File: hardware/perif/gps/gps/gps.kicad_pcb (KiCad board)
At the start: 2 copper layers, 37 x 53 mm, 5 parts, among them J1 Conn_01x20_Male, U1 M10578-A2

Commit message: started GPS board skeleton
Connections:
- U1 pad 10: Net-(J1-Pad16) -> Net-(J1-Pad17)
- U1 pad 9: Net-(J1-Pad17) -> Net-(J1-Pad16)
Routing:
- net Net-(J1-Pad17): track 4.81 -> 8.73 mm
- net Net-(J1-Pad16): track 5.21 -> 6.11 mm
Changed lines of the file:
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@@
     (thickness 1.6)
     (drawings 4)
-    (tracks 165)
+    (tracks 174)
     (zones 0)
     (modules 5)
@@
     (fp_line (start -4.5 -4.5) (end -4.5 4.5) (layer F.SilkS) (width 0.15))
     (pad 10 smd rect (at 1.85 3.7 270) (size 1 1) (layers F.Cu F.Paste F.Mask)
+      (net 2 "Net-(J1-Pad17)"))
+    (pad 9 smd rect (at 3.7 3.7 270) (size 1 1) (layers F.Cu F.Paste F.Mask)
       (net 3 "Net-(J1-Pad16)"))
-    (pad 9 smd rect (at 3.7 3.7 270) (size 1 1) (layers F.Cu F.Paste F.Mask)
-      (net 2 "Net-(J1-Pad17)"))
     (pad 8 smd rect (at 3.7 1.85 270) (size 1 1) (layers F.Cu F.Paste F.Mask)
       (net 18 "Net-(U1-Pad8)"))
@@
   (segment (start 74.252081 68.45) (end 74.342081 68.54) (width 0.15) (layer F.Cu) (net 2))
   (segment (start 73.05 68.45) (end 74.252081 68.45) (width 0.15) (layer F.Cu) (net 2))
-  (segment (start 74.342081 68.54) (end 77.82 68.54) (width 0.15) (layer F.Cu) (net 2))
-  (segment (start 77.92 66.73) (end 73.74 66.73) (width 0.15) (layer F.Cu) (net 3))
+  (segment (start 78.645001 69.260001) (end 78.645001 67.575001) (width 0.15) (layer F.Cu) (net 2))
+  (segment (start 78.600001 69.305001) (end 78.645001 69.260001) (width 0.15) (layer F.Cu) (net 2))
+  (segment (start 77.177721 69.305001) (end 78.600001 69.305001) (width 0.15) (layer F.Cu) (net 2))
+  (segment (start 76.41272 68.54) (end 77.177721 69.305001) (width 0.15) (layer F.Cu) (net 2))
+  (segment (start 74.342081 68.54) (end 76.41272 68.54) (width 0.15) (layer F.Cu) (net 2))
+  (segment (start 78.645001 67.575001) (end 77.88 66.81) (width 0.15) (layer F.Cu) (net 2))
   (segment (start 73.74 66.73) (end 73.01 66) (width 0.15) (layer F.Cu) (net 3))
+  (segment (start 73.814999 67.264999) (end 75.561997 67.264999) (width 0.15) (layer F.Cu) (net 3))
+  (segment (start 75.561997 67.264999) (end 77.036998 68.74) (width 0.15) (layer F.Cu) (net 3))
+  (segment (start 73.74 67.19) (end 73.814999 67.264999) (width 0.15) (layer F.Cu) (net 3))
+  (segment (start 73.74 66.73) (end 73.74 67.19) (width 0.15) (layer F.Cu) (net 3))
+  (segment (start 77.036998 68.74) (end 77.72 68.74) (width 0.15) (layer F.Cu) (net 3))
   (segment (start 85.32 64.88) (end 91.87 64.88) (width 0.15) (layer F.Cu) (net 15))
   (segment (start 91.87 64.88) (end 96.53 69.54) (width 0.15) (layer F.Cu) (net 15))

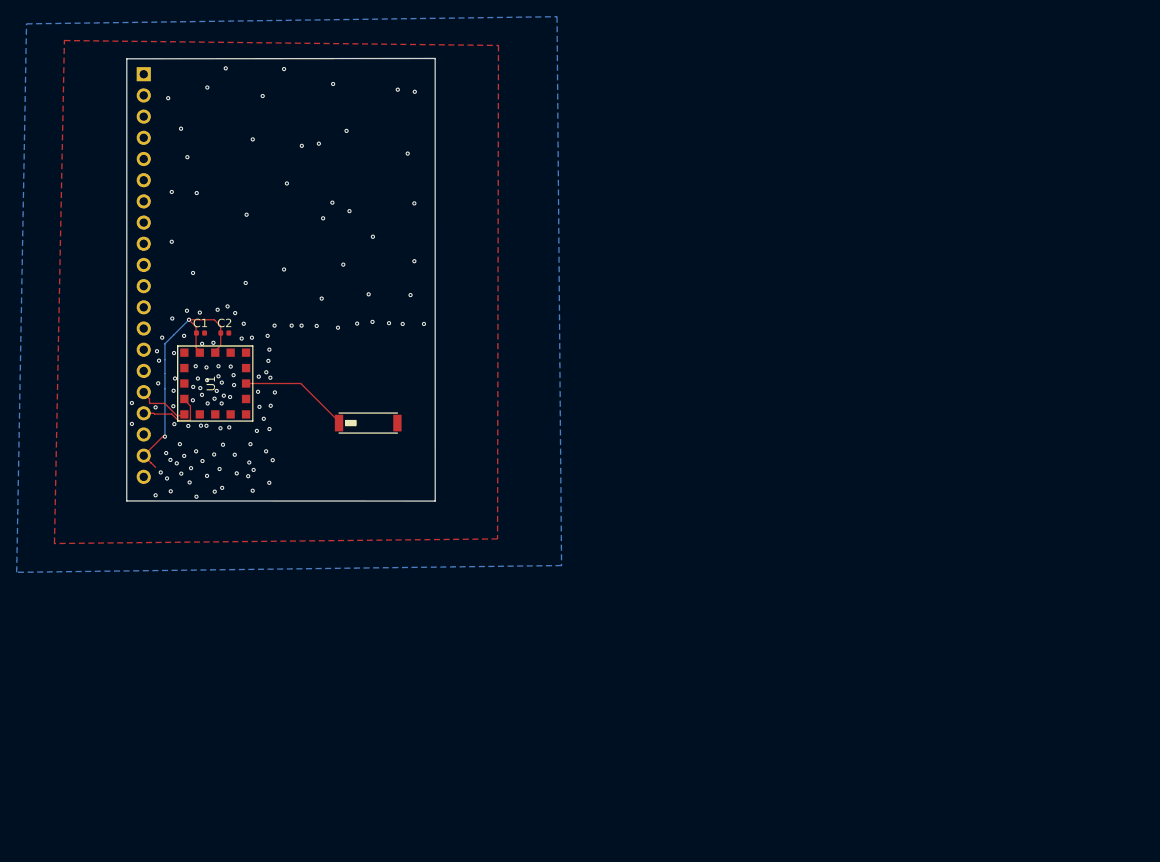
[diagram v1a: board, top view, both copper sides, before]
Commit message: u-blox GPS CAM-M8Q
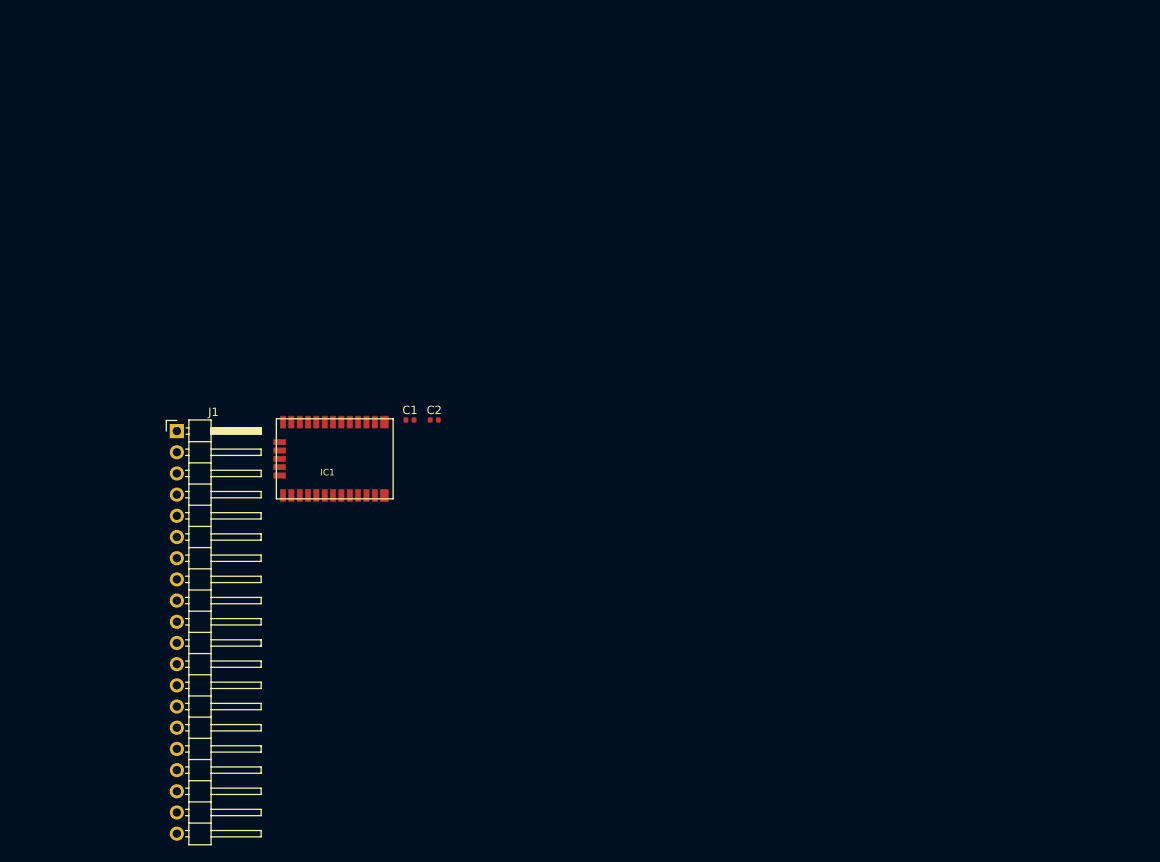
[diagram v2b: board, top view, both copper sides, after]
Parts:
- removed AE1: Antenna_Chip, kifootp:575AT43A40
- removed U1: M10578-A2, kifootp:M10578-A3
- added IC1: CAM-M8Q, kifootp:CAM-M8Q, F.Cu at (95.9, 73.9)
- J1: moved to F.Cu
- moved J1 43.0 mm to (77.0, 70.6), turned to 0 degrees
- moved C2 27.2 mm to (107.9, 69.2)
- moved C1 27.2 mm to (105.0, 69.2)
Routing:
- net Net-(C1-Pad1): track 32.7 -> 0.00 mm, vias 2 -> 0
- net Net-(AE1-Pad1): track 13.1 -> 0.00 mm
- net Net-(IC1-Pad25): track 8.73 -> 0.00 mm
- net Net-(IC1-Pad26): track 6.11 -> 0.00 mm
- net Net-(C1-Pad2): vias 136 -> 0
- removed copper zone on B.Cu, net Net-(C1-Pad2)
- removed copper zone on F.Cu, net Net-(C1-Pad2)
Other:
- board outline removed

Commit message: u-blox GPS CAM-M8Q
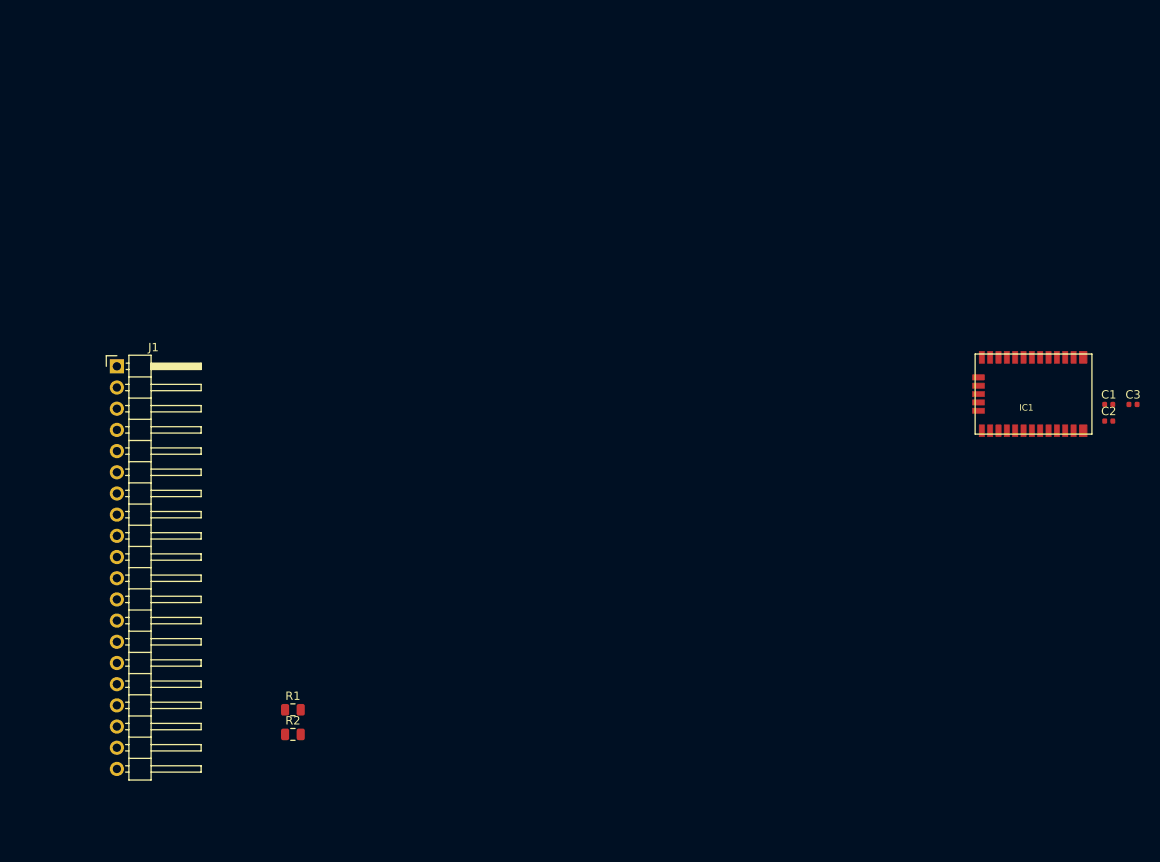
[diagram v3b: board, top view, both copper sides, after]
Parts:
- added C3: C, Capacitor_SMD:C_0402_1005Metric, F.Cu at (191.6, 67.4)
- added R1: 200, Resistor_SMD:R_0805_2012Metric, F.Cu at (90.9, 104.0)
- added R2: 200, Resistor_SMD:R_0805_2012Metric, F.Cu at (90.9, 106.9)
- moved IC1 84.1 mm to (179.7, 66.1)
- moved C1 83.8 mm to (188.7, 67.4)
- moved C2 80.9 mm to (188.7, 69.4)
- moved J1 10.6 mm to (69.8, 62.8)
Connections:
- net Net-(C1-Pad1) renamed +3V3
- net Net-(C1-Pad2) renamed GND
- J1 pad 16: Net-(IC1-Pad26) -> master_tx
- J1 pad 17: Net-(IC1-Pad25) -> master_rx
